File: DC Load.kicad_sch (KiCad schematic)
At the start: 119 parts, among them IC1 REF7050QDGKR, IC10 REF7050QDGKR, IC11 ISO7740FQDBQRQ1, IC12 ISO7741FQDBQRQ1, IC13 INA826AID, IC14 OPA210IDGKR, IC15 INA296A3IDDFR, IC16 MAX31850K, IC17 ISO7741FQDBQRQ1, IC18 ISO7741FQDBQRQ1, IC2 MAX5719GSD+, IC3 REF7050QDGKR, IC4 AD7175-2BRUZ, IC5 OPA210IDGKR, IC6 L78L33ACD13TR, IC7 L78L33ACD13TR, IC8 L78L06ACD13TR, IC9 L78L05ACD13TR, J2 Conn_01x06, J3 Fan, J4 Power In, J5 1904147, J7 UI, Q1 MSC017SMA120B4N, U1 DI79L05UAB

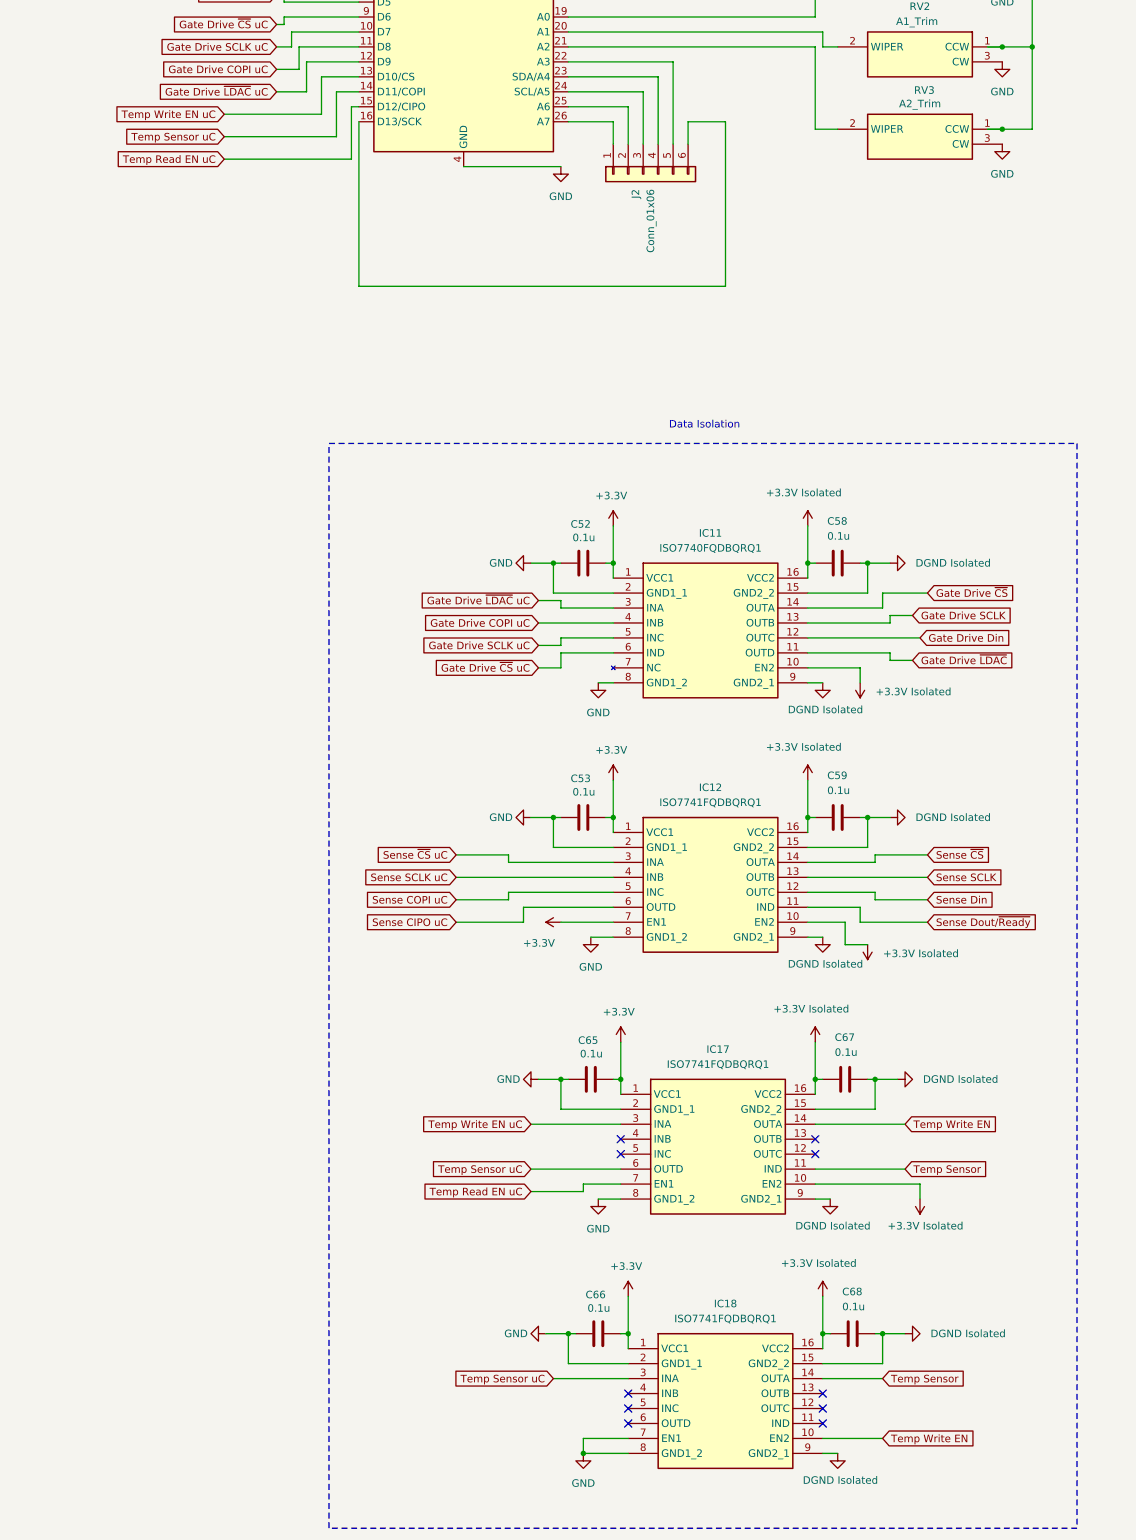
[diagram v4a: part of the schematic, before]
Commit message: improved the connection to the temp sensor
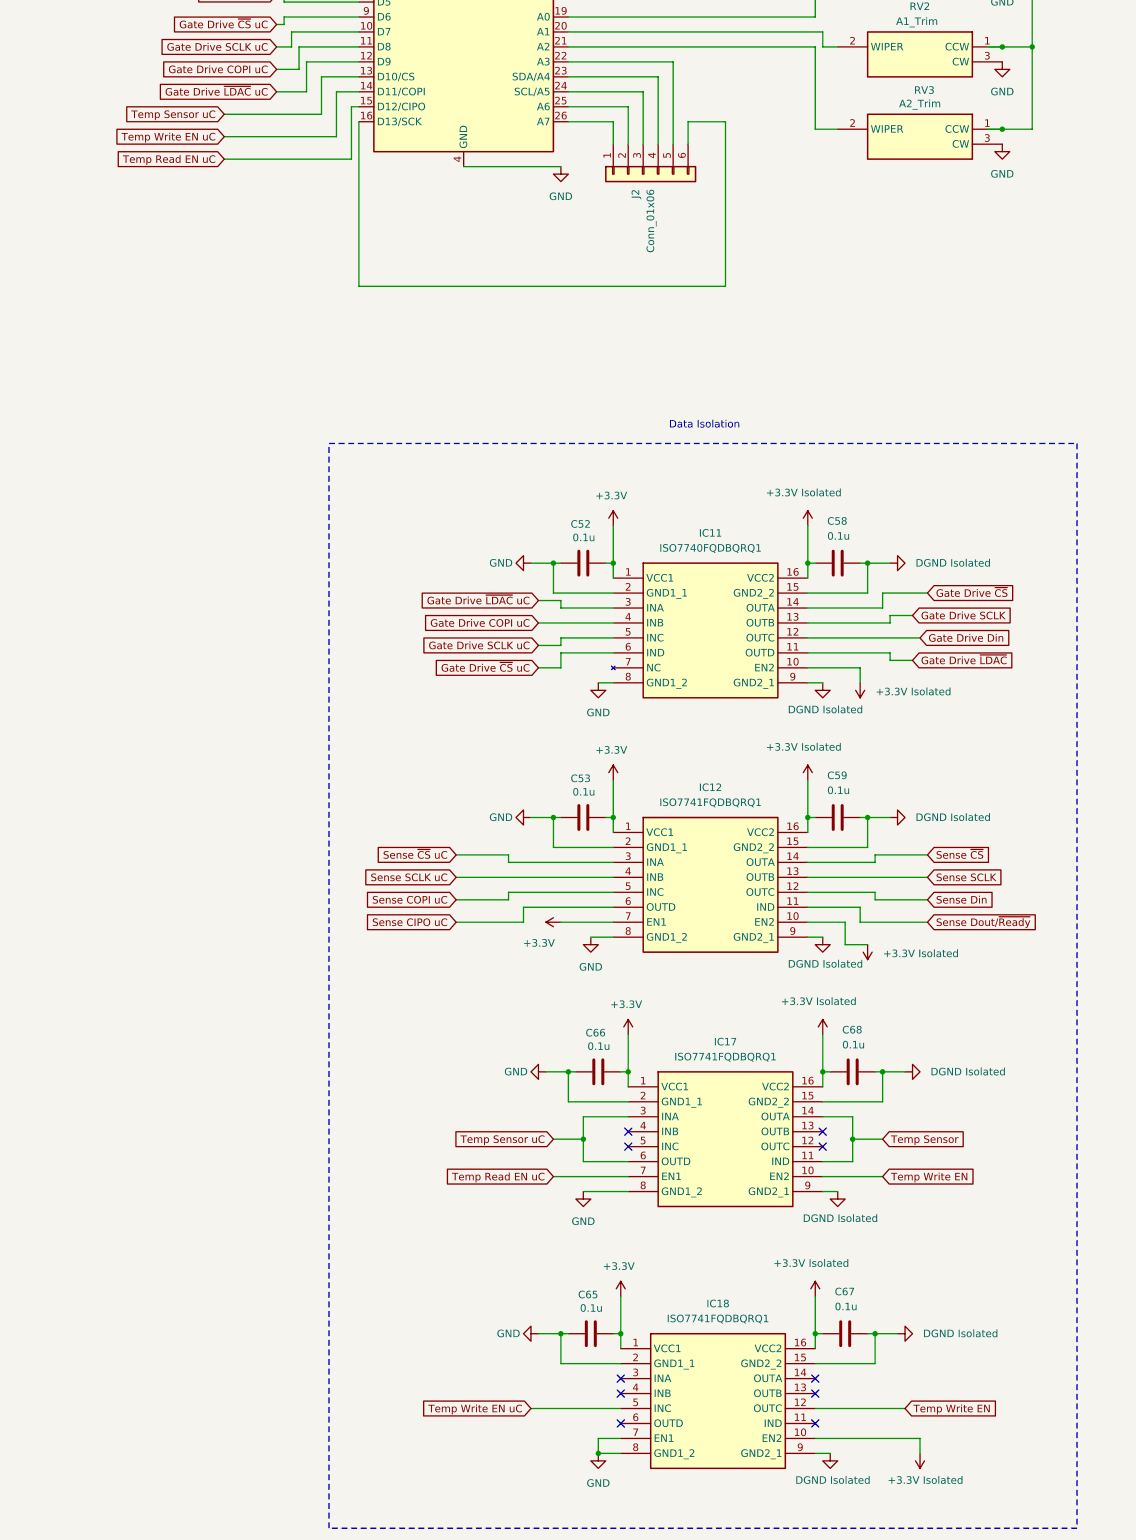
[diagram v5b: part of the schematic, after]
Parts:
- renumbered IC18 to IC17, IC17 to IC18
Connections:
- net GND: now also IC18.7 (EN1); no longer IC17.7 (EN1)
- net Temp Read EN uC: now also IC17.7 (EN1); no longer IC18.7 (EN1)
- net Temp Sensor: now also IC17.11 (IND); no longer IC18.11 (IND)
- net Temp Sensor uC: now also A1.13 (D10/CS), IC17.6 (OUTD); no longer A1.14 (D11/COPI), IC18.6 (OUTD)
- net Temp Write EN: now also IC18.12 (OUTC); no longer IC18.14 (OUTA)
- net Temp Write EN uC: now also A1.14 (D11/COPI), IC18.5 (INC); no longer A1.13 (D10/CS), IC18.3 (INA)
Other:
- moved on the sheet: C65, C66, C67, C68, IC17, IC18

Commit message: added test points
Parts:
- removed C10: 1u, Capacitor_SMD:C_1206_3216Metric, symbol Device:C
- removed C14: .1u, Capacitor_SMD:C_0603_1608Metric, symbol Device:C
- removed NT3: NetTie_2, NetTie:NetTie-2_SMD_Pad2.0mm, symbol Device:NetTie_2
- added TP1, TP10, TP11, TP2, TP26, TP27, TP28, TP29, TP3, TP30, TP31, TP32, TP33, TP34, TP35, TP36, TP37, TP38, TP4, TP5, TP6, TP7, TP8, TP9: TestPoint, TestPoint:TestPoint_Pad_SMD-0603, symbol Connector:TestPoint
- added TP12, TP13, TP14, TP15, TP16, TP17, TP18, TP19, TP20, TP21, TP22, TP23, TP24, TP25: TestPoint, TestPoint:TestPoint_Keystone_5010-5014_Multipurpose, symbol Connector:TestPoint
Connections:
- net DGND Isolated is gone; now on net GND Isolated: C12.2, C42.1, C43.2, C44.1, C45.2, C58.2, C59.2, C67.2, C68.2, IC11.15 (GND2_2), IC11.9 (GND2_1), IC12.15 (GND2_2), IC12.9 (GND2_1), IC16.3 (GND), IC17.15 (GND2_2), IC17.9 (GND2_1), IC18.15 (GND2_2), IC18.9 (GND2_1), IC2.12 (DGND), IC4.17 (DGND)
- net Current Sense +: now also TP34.1
- net Current Sense -: now also TP33.1
- net Current Sense Amp Out: now also TP11.1
- net GND: now also TP12.1, TP13.1, TP14.1, TP15.1, TP16.1, TP17.1
- net GND Isolated: now also TP18.1, TP19.1, TP20.1, TP21.1, TP22.1, TP23.1, TP24.1, TP25.1
- net Gate Drive +: now also TP37.1
- net Gate Drive -: now also TP38.1
- net Gate Drive Din: now also TP27.1
- net Gate Drive SCLK: now also TP28.1
- net Gate Drive ~{CS}: now also TP26.1
- net Gate Drive ~{LDAC}: now also TP29.1
- net Sense Amp Ref: now also TP30.1, TP31.1, TP32.1
- net Sense Din: now also TP6.1
- net Sense Dout/~{Ready}: now also TP8.1
- net Sense SCLK: now also TP9.1
- net Sense ~{CS}: now also TP7.1
- net Temp Read EN uC: now also TP4.1
- net Temp Sensor: now also TP1.1
- net Temp Sensor uC: now also TP2.1
- net Temp Write EN: now also TP3.1
- net Temp Write EN uC: now also TP5.1
- net Voltage Sense +: now also TP36.1
- net Voltage Sense -: now also TP35.1
- net Voltage Sense Amp Out: now also TP10.1

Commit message: added 3D models
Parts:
- IC13: footprint INA296A3IDDFR:SOT65P280X110-8N -> INA826AID:SOIC127P600X175-8N
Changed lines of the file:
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@@
 			)
 		)
-		(property "Footprint" "INA296A3IDDFR:SOT65P280X110-8N"
+		(property "Footprint" "INA826AID:SOIC127P600X175-8N"
 			(at 520.7 239.7 0)
 			(effects

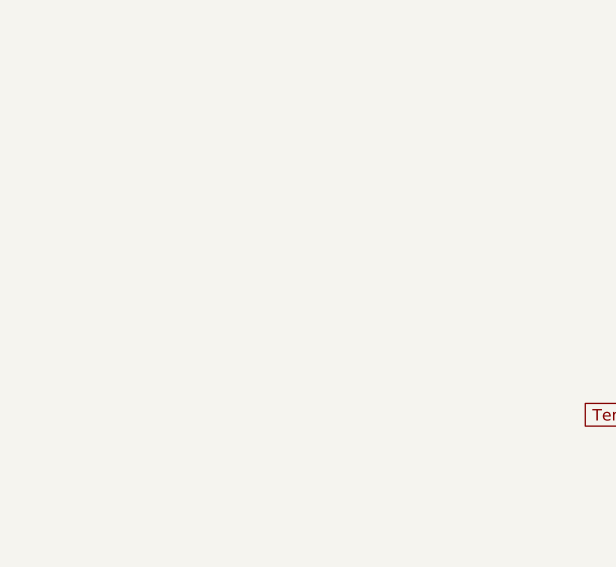
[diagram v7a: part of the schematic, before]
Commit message: added the rest of the 3D models. Added logo
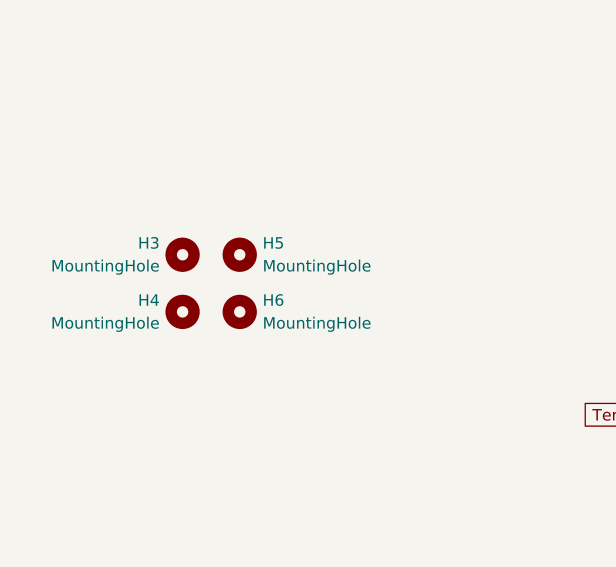
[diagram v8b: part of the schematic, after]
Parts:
- added H3, H4, H5, H6: MountingHole, MountingHole:MountingHole_3.2mm_M3, symbol Mechanical:MountingHole
- J2: footprint Connector_PinHeader_2.54mm:PinHeader_1x06_P2.54mm_Vertical -> Connector_PinSocket_2.54mm:PinSocket_1x06_P2.54mm_Vertical
